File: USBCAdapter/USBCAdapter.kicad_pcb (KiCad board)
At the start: 2 copper layers, 27 x 24 mm, 21 parts, among them J1 USB_C_Receptacle_USB2.0_16P, J2 Conn_01x02, J4 Conn_01x04_MountingPin, U1 TP4057, U2 TP4057

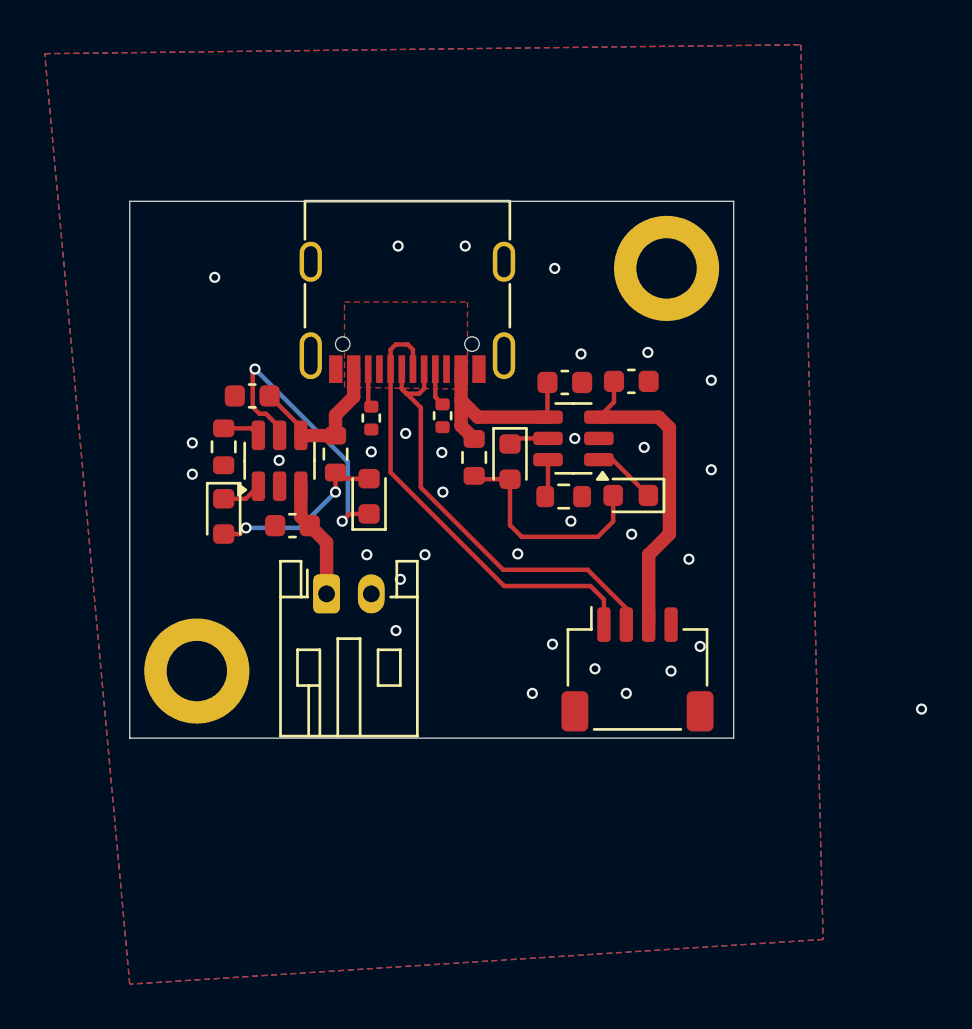
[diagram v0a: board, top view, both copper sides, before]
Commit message: switched back to onboard charger and the most boring adapter board ever
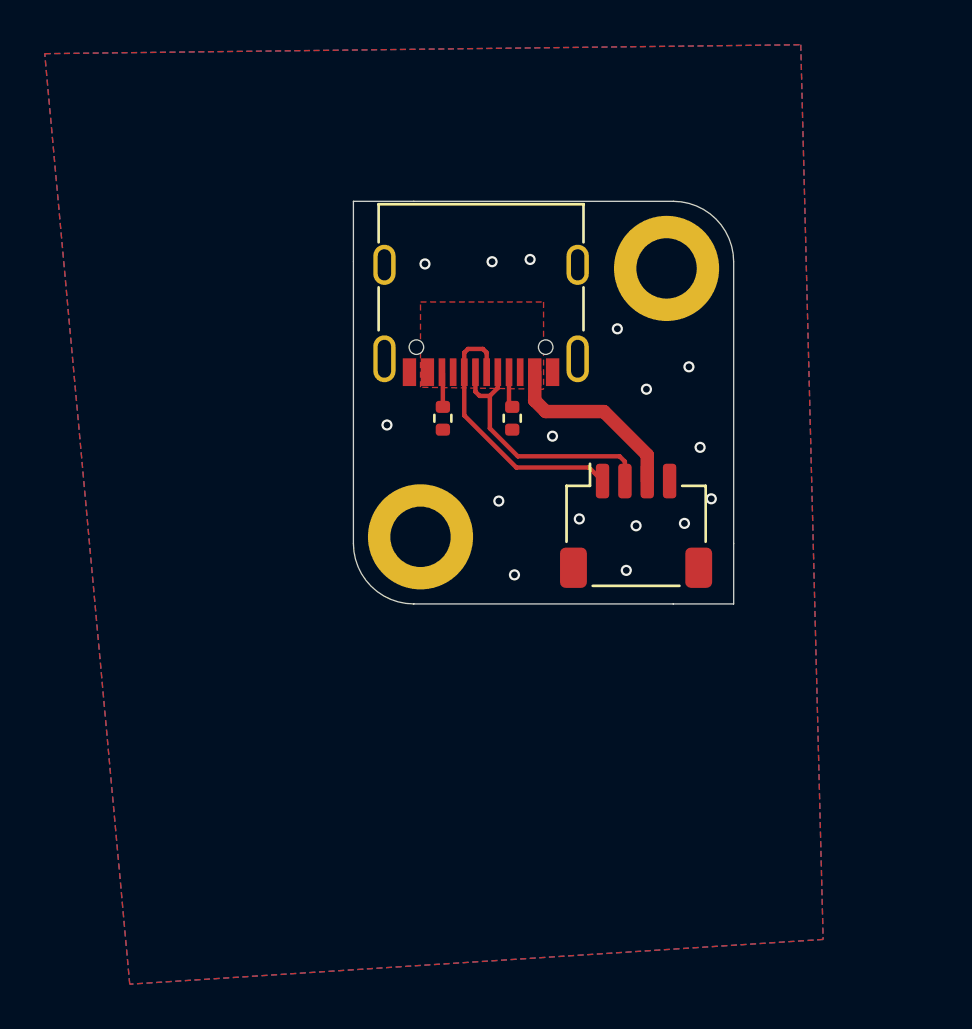
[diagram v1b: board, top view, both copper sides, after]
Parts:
- removed C1, C4: 1uF, Capacitor_SMD:C_0603_1608Metric
- removed C2, C3: 10uF, Capacitor_SMD:C_0603_1608Metric
- removed D1, D2, D3, D4: LED, LED_SMD:LED_0603_1608Metric
- removed J2: Conn_01x02, Connector_JST:JST_PH_S2B-PH-K_1x02_P2.00mm_Horizontal
- removed R3, R5: 1k, Resistor_SMD:R_0603_1608Metric
- removed R4, R6: 1.8k, Resistor_SMD:R_0603_1608Metric
- removed U1, U2: TP4057, Package_TO_SOT_SMD:TSOT-23-6
- moved H2 11.7 mm to (56.0, 55.0)
- moved J4 6.42 mm to (65.6, 54.5)
- moved J1 3.30 mm to (58.7, 43.9)
- moved R2 3.20 mm to (57.0, 49.7)
- moved R1 3.11 mm to (60.1, 49.7)
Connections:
- J4 pad 3: /V_CHARGE -> VBUS
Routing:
- net /V_CHARGE: track 14.4 -> 0.00 mm
- net Net-(D3-K): track 13.6 -> 0.00 mm, vias 2 -> 0
- net Net-(D1-A): track 9.99 -> 0.00 mm
- net /D+: track 20.6 -> 12.2 mm
- net Net-(D3-A): track 8.27 -> 0.00 mm, vias 2 -> 0
- net /D-: track 19.9 -> 11.8 mm
- net VBUS: track 16.4 -> 8.48 mm
- net Net-(J2-Pin_1): track 5.29 -> 0.00 mm
- net Net-(D1-K): track 2.88 -> 0.00 mm
- net Net-(D2-K): track 1.80 -> 0.00 mm
- net Net-(D4-K): track 1.78 -> 0.00 mm
- net Net-(U1-PROG): track 1.70 -> 0.00 mm
- net Net-(U2-PROG): track 1.68 -> 0.00 mm
- net GND: vias 32 -> 16
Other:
- board size 27 x 24 mm -> 17 x 18 mm
